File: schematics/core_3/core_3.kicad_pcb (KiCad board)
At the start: 2 copper layers, 100 x 91.1 mm, 14 parts

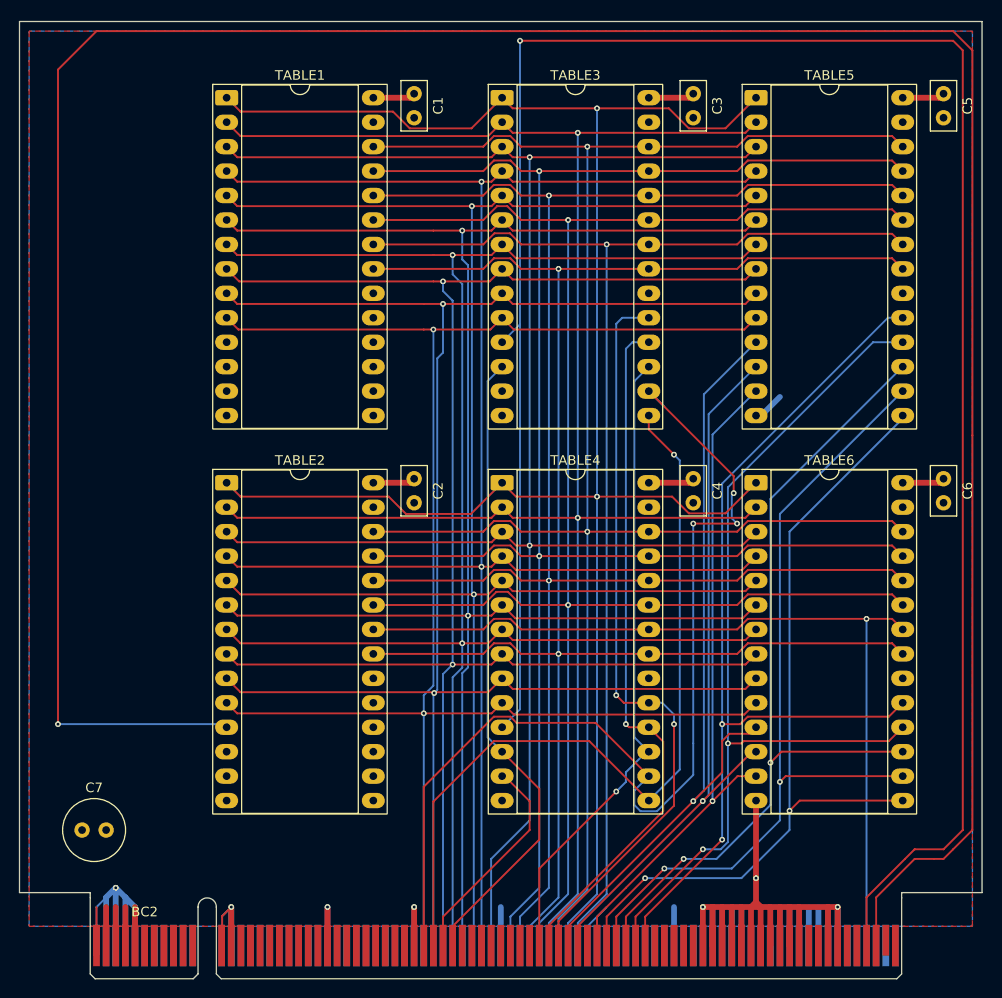
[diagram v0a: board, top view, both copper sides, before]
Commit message: Add pcb for core 3
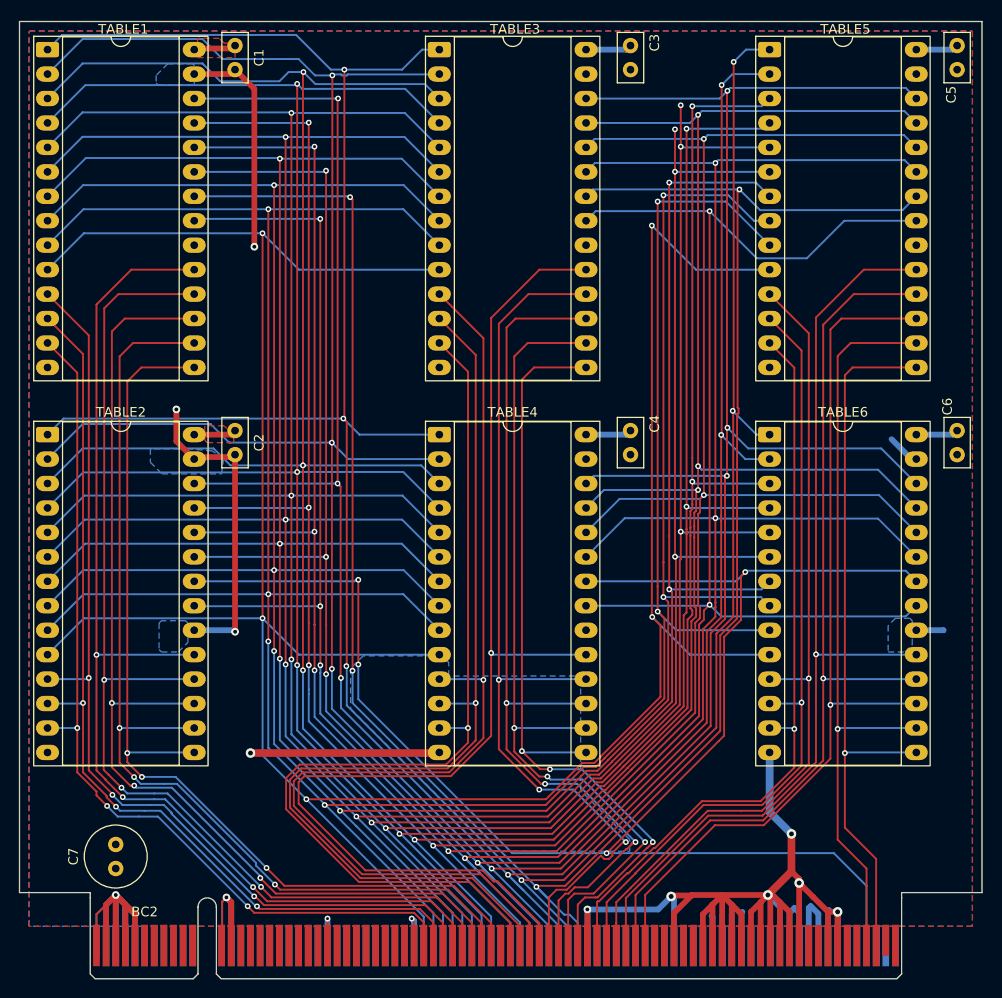
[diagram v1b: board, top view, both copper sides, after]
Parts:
- moved C1 19.3 mm to (75.4, 55.5)
- moved C2 19.3 mm to (75.4, 95.5)
- moved TABLE1 19.3 mm to (55.9, 55.9)
- moved TABLE2 19.3 mm to (55.9, 95.9)
- moved C3 8.22 mm to (116.5, 55.5)
- moved C4 8.22 mm to (116.5, 95.5)
- moved TABLE3 8.22 mm to (96.6, 55.9)
- moved TABLE4 8.22 mm to (96.6, 95.9)
- moved C7 5.32 mm to (63.0, 141.0), turned to 90 degrees
- moved C5 5.20 mm to (150.4, 55.5)
- moved C6 5.20 mm to (150.4, 95.5)
- moved TABLE5 5.20 mm to (130.9, 55.9)
- moved TABLE6 5.20 mm to (130.9, 95.9)
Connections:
- BC2 pad A41: GND -> (no net)
- BC2 pad B33: Net-(BC2-L0) -> /L0
- BC2 pad B34: Net-(BC2-L1) -> /L1
- BC2 pad B35: Net-(BC2-L2) -> /L2
- BC2 pad B36: Net-(BC2-L3) -> /L3
- BC2 pad B40: Net-(BC2-R0) -> /R0
- BC2 pad B41: GND -> (no net)
- BC2 pad B42: Net-(BC2-R1) -> /R1
- BC2 pad B43: Net-(BC2-R2) -> /R2
- BC2 pad B44: Net-(BC2-R3) -> /R3
- BC2 pad B79: Net-(BC2-L4) -> /L4
- BC2 pad B80: Net-(BC2-R4) -> /R4
- TABLE1 pad 11: Net-(BC2-R4) -> /L2
- TABLE1 pad 12: Net-(BC2-R3) -> /L1
- TABLE1 pad 13: Net-(BC2-R2) -> /L0
- TABLE1 pad 15: Net-(BC2-R1) -> /R0
- TABLE1 pad 16: Net-(BC2-R0) -> /~{FlagsUpdate}
- TABLE1 pad 17: /ALUM -> /~{ALUCarryIn}
- TABLE1 pad 18: /~{ALUCarryIn} -> /ALUM
- TABLE1 pad 19: /~{FlagsUpdate} -> /L3
- TABLE2 pad 11: Net-(BC2-R4) -> /L2
- TABLE2 pad 12: Net-(BC2-R3) -> /L1
- TABLE2 pad 13: Net-(BC2-R2) -> /L0
- TABLE2 pad 15: Net-(BC2-R1) -> /R0
- TABLE2 pad 16: Net-(BC2-R0) -> /~{FlagsUpdate}
- TABLE2 pad 17: /ALUM -> /~{ALUCarryIn}
- TABLE2 pad 18: /~{ALUCarryIn} -> /ALUM
- TABLE2 pad 19: /~{FlagsUpdate} -> /L3
- TABLE3 pad 11: Net-(BC2-L4) -> /R3
- TABLE3 pad 12: Net-(BC2-L3) -> /R2
- TABLE3 pad 13: Net-(BC2-L2) -> /R1
- TABLE3 pad 15: Net-(BC2-L1) -> /ALUS1
- TABLE3 pad 16: Net-(BC2-L0) -> /ALUS0
- TABLE3 pad 17: /~{SCClear} -> /PCIncrement
- TABLE3 pad 19: /PCIncrement -> /~{SCClear}
- TABLE4 pad 11: Net-(BC2-L4) -> /R3
- TABLE4 pad 12: Net-(BC2-L3) -> /R2
- TABLE4 pad 13: Net-(BC2-L2) -> /R1
- TABLE4 pad 15: Net-(BC2-L1) -> /ALUS1
- TABLE4 pad 16: Net-(BC2-L0) -> /ALUS0
- TABLE4 pad 17: /~{SCClear} -> /PCIncrement
- TABLE4 pad 19: /PCIncrement -> /~{SCClear}
- TABLE5 pad 11: /ALUS0 -> /SPDecrement
- TABLE5 pad 12: /ALUS1 -> /ALUS3
- TABLE5 pad 15: /ALUS3 -> /R4
- TABLE5 pad 16: /SPDecrement -> /L4
- TABLE5 pad 17: /SPIncrement -> /AccumShiftRight
- TABLE5 pad 19: /AccumShiftRight -> /SPIncrement
- TABLE6 pad 11: /ALUS0 -> /SPDecrement
- TABLE6 pad 12: /ALUS1 -> /ALUS3
- TABLE6 pad 15: /ALUS3 -> /R4
- TABLE6 pad 16: /SPDecrement -> /L4
- TABLE6 pad 17: /SPIncrement -> /AccumShiftRight
- TABLE6 pad 19: /AccumShiftRight -> /SPIncrement
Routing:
- net Net-(BC2-R4): track 282.0 -> 0.00 mm, vias 1 -> 0
- net Net-(BC2-L4): track 220.0 -> 0.00 mm, vias 1 -> 0
- net /L3: track 0.00 -> 116.2 mm, vias 0 -> 3
- net GND: track 170.9 -> 286.5 mm, vias 6 -> 13
- net /ALUM: track 0.00 -> 113.5 mm, vias 0 -> 3
- net /~{ALUCarryIn}: track 0.00 -> 109.5 mm, vias 0 -> 3
- net /STATE0: track 178.4 -> 287.3 mm, vias 2 -> 5
- net /R3: track 0.00 -> 108.6 mm, vias 0 -> 1
- net /STATE1: track 181.0 -> 289.2 mm, vias 2 -> 6
- net /STATE5: track 190.9 -> 298.7 mm, vias 2 -> 7
- net Net-(BC2-L0): track 107.7 -> 0.00 mm, vias 3 -> 0
- net /STATE4: track 188.7 -> 295.4 mm, vias 2 -> 7
- net /~{FlagsUpdate}: track 0.00 -> 105.3 mm, vias 0 -> 3
- net /STATE2: track 183.6 -> 288.9 mm, vias 2 -> 6
- net /STATE6: track 193.3 -> 298.1 mm, vias 2 -> 6
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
